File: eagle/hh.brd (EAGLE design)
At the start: 169.7 x 51.9 mm, 7 parts

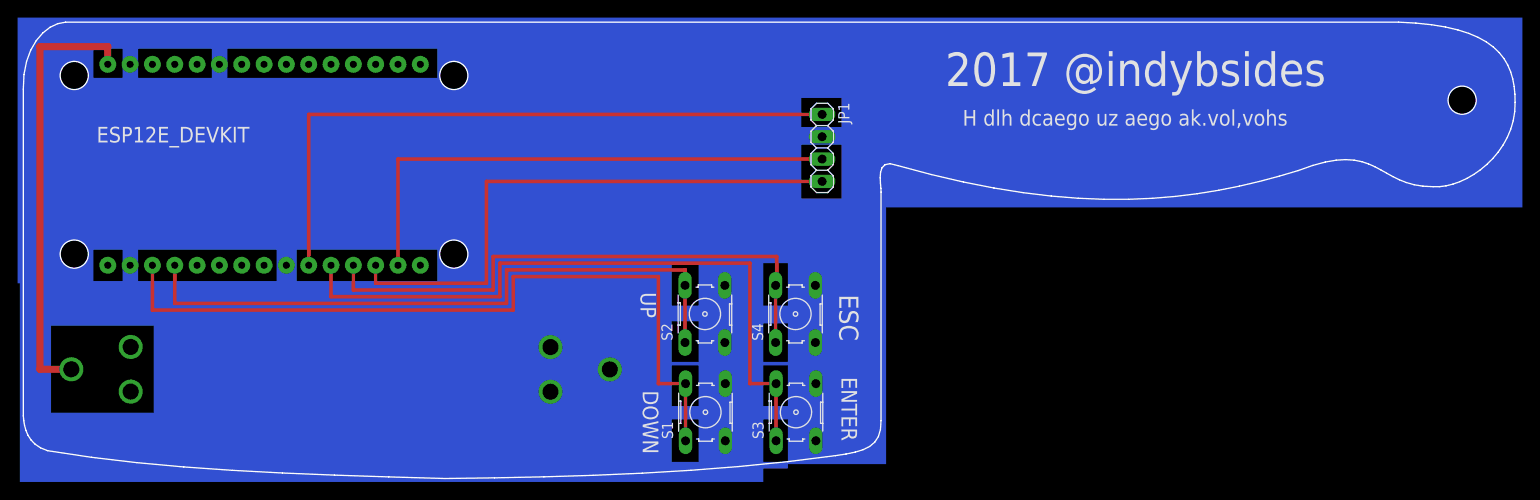
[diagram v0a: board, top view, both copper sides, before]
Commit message: Major changes to placement of components
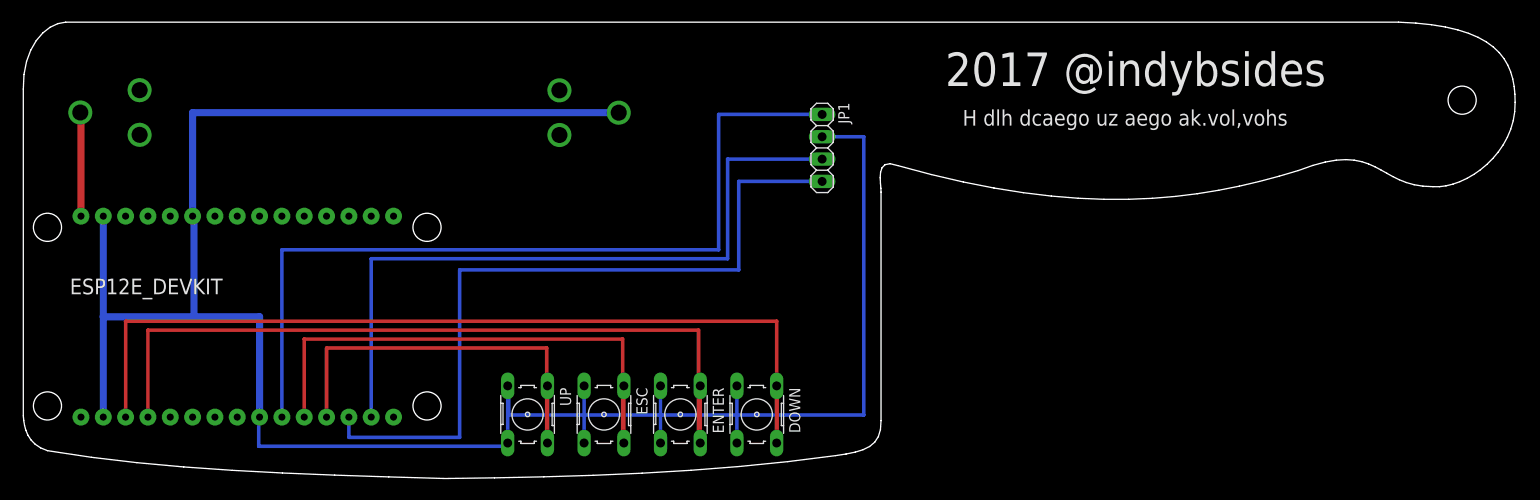
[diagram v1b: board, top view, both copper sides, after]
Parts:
- removed S1, S2, S3, S4: (no value), switch-omron:B3F-10XX
- added DOWN, ENTER, ESC, UP: (no value), switch-omron:B3F-10XX
- moved BAT1 29.2 mm to (37.3, 41.8)
- moved ESP12E_DEVKIT 17.5 mm to (24.5, 18.6)
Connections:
- net N$1: now also DOWN.3, DOWN.4, ENTER.3, ENTER.4, ESC.3, ESC.4, UP.3, UP.4; no longer S1.3, S1.4, S2.3, S2.4, S3.3, S3.4, S4.3, S4.4
- net N$2: now also UP.1, UP.2; no longer S4.1, S4.2
- net N$7: now also ESC.1, ESC.2; no longer S3.1, S3.2
- net N$8: now also ENTER.1, ENTER.2; no longer S2.1, S2.2
- net N$9: now also DOWN.1, DOWN.2; no longer S1.1, S1.2
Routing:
- net N$4: track 50.0 -> 11.9 mm
- net N$6: track 64.4 -> 85.3 mm
- net N$5: track 60.3 -> 80.6 mm
- net N$3: track 75.6 -> 95.9 mm
- net N$8: track 74.5 -> 92.1 mm
- net N$9: track 88.2 -> 105.3 mm
- net N$7: track 78.2 -> 63.6 mm
- net N$2: track 64.7 -> 50.3 mm
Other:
- board text removed: "DOWN"
- board text removed: "ENTER"
- board text removed: "ESC"
- board text removed: "UP"

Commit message: Trace Revisions
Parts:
- removed BAT1: (no value), SparkFun-Electromechanical:BATTERY_18650-HOLDER
- added BT1: (no value), SF_Batteries:BATTERY_18650-HOLDER
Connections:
- net N$1: now also BT1.GND@1; no longer BAT1.GND@1
- net N$4: now also BT1.PWR@1; no longer BAT1.PWR@1
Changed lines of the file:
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@@
 <layer number="113" name="IDFDebug" color="4" fill="1" visible="yes" active="yes"/>
 <layer number="116" name="Patch_BOT" color="9" fill="4" visible="yes" active="yes"/>
+<layer number="118" name="Rect_Pads" color="7" fill="1" visible="yes" active="yes"/>
 <layer number="121" name="_tsilk" color="7" fill="1" visible="yes" active="yes"/>
 <layer number="122" name="_bsilk" color="7" fill="1" visible="yes" active="yes"/>
@@
 <element name="ESP12E_DEVKIT" library="ESP12E_DEVKIT" package="ESP12E_DEVKIT" value="ESP12E_DEVKIT" x="24.482" y="18.558" rot="R270"/>
 <element name="JP1" library="pinhead" package="1X04" value="OLED" x="91.02" y="37.75" rot="R270"/>
-<element name="BAT1" library="SparkFun-Electromechanical" package="BATTERY_18650-HOLDER" value="" x="37.254" y="41.77" rot="SMR180"/>
+<element name="BT1" library="SF_Batteries" package="BATTERY_18650-HOLDER" value="" x="37.338" y="42.164" rot="SMR180">
+<attribute name="PROD_ID" value="BATT-12327" x="37.338" y="42.164" size="1.778" layer="28" rot="SMR180" display="off"/>
+<attribute name="SF_SKU" value="PRT-13113" x="37.338" y="42.164" size="1.778" layer="28" rot="SMR180" display="off"/>
+</element>
 </elements>
 <signals>
@@
 <contactref element="ESC" pad="4"/>
 <contactref element="UP" pad="4"/>
-<contactref element="BAT1" pad="GND@1"/>
 <wire x1="63.9414" y1="10.6812" x2="63.9414" y2="4.1788" width="0.4064" layer="16"/>
 <wire x1="81.3254" y1="7.366" x2="81.3254" y2="10.6812" width="0.4064" layer="16"/>
@@
 <wire x1="55.2494" y1="4.1788" x2="55.2494" y2="10.6812" width="0.4064" layer="16"/>
 <wire x1="9.242" y1="7.128" x2="9.242" y2="18.542" width="0.8128" layer="16"/>
-<wire x1="19.402" y1="29.988" x2="19.558" y2="29.988" width="0.4064" layer="16"/>
-<wire x1="19.558" y1="29.988" x2="19.558" y2="18.542" width="0.8128" layer="16"/>
-<wire x1="19.558" y1="18.542" x2="9.242" y2="18.542" width="0.8128" layer="16"/>
+<wire x1="19.402" y1="29.988" x2="19.304" y2="29.988" width="0.4064" layer="16"/>
+<wire x1="19.304" y1="29.988" x2="19.304" y2="18.542" width="0.8128" layer="16"/>
+<wire x1="19.304" y1="18.542" x2="9.242" y2="18.542" width="0.8128" layer="16"/>
 <wire x1="9.242" y1="18.542" x2="9.242" y2="29.988" width="0.8128" layer="16"/>
-<wire x1="19.558" y1="18.542" x2="27.022" y2="18.542" width="0.8128" layer="16"/>
+<wire x1="19.304" y1="18.542" x2="27.022" y2="18.542" width="0.8128" layer="16"/>
 <wire x1="27.022" y1="18.542" x2="27.022" y2="7.128" width="0.8128" layer="16"/>
 <wire x1="55.2494" y1="10.6812" x2="55.372" y2="10.6812" width="0.4064" layer="16"/>
@@
 <wire x1="95.758" y1="39.02" x2="95.758" y2="7.366" width="0.4064" layer="16"/>
 <wire x1="95.758" y1="7.366" x2="81.3254" y2="7.366" width="0.4064" layer="16"/>
-<wire x1="67.882" y1="41.76" x2="19.402" y2="41.76" width="0.8128" layer="16"/>
-<wire x1="19.402" y1="41.76" x2="19.402" y2="29.988" width="0.8128" layer="16"/>
+<contactref element="BT1" pad="GND@1"/>
+<wire x1="67.966" y1="42.154" x2="67.818" y2="42.154" width="0.4064" layer="1"/>
+<wire x1="67.818" y1="42.154" x2="67.818" y2="33.782" width="0.8128" layer="1"/>
+<wire x1="67.818" y1="33.782" x2="19.402" y2="33.782" width="0.8128" layer="1"/>
+<wire x1="19.402" y1="33.782" x2="19.402" y2="29.988" width="0.8128" layer="1"/>
 <wire x1="63.9414" y1="10.6812" x2="72.6334" y2="10.6812" width="0" layer="19" extent="1-1"/>
 <wire x1="55.372" y1="10.6812" x2="63.9414" y2="10.6812" width="0" layer="19" extent="16-16"/>
 </signal>
 <signal name="N$4">
-<contactref element="BAT1" pad="PWR@1"/>
+<contactref element="BT1" pad="PWR@1"/>
 <contactref element="ESP12E_DEVKIT" pad="VIN"/>
-<wire x1="6.626" y1="41.78" x2="6.702" y2="41.78" width="0.8128" layer="1"/>
-<wire x1="6.702" y1="41.78" x2="6.702" y2="29.988" width="0.8128" layer="1"/>
+<wire x1="6.71" y1="42.174" x2="6.702" y2="42.174" width="0.4064" layer="1"/>
+<wire x1="6.702" y1="42.174" x2="6.702" y2="29.988" width="0.8128" layer="1"/>
 </signal>
 </signals>

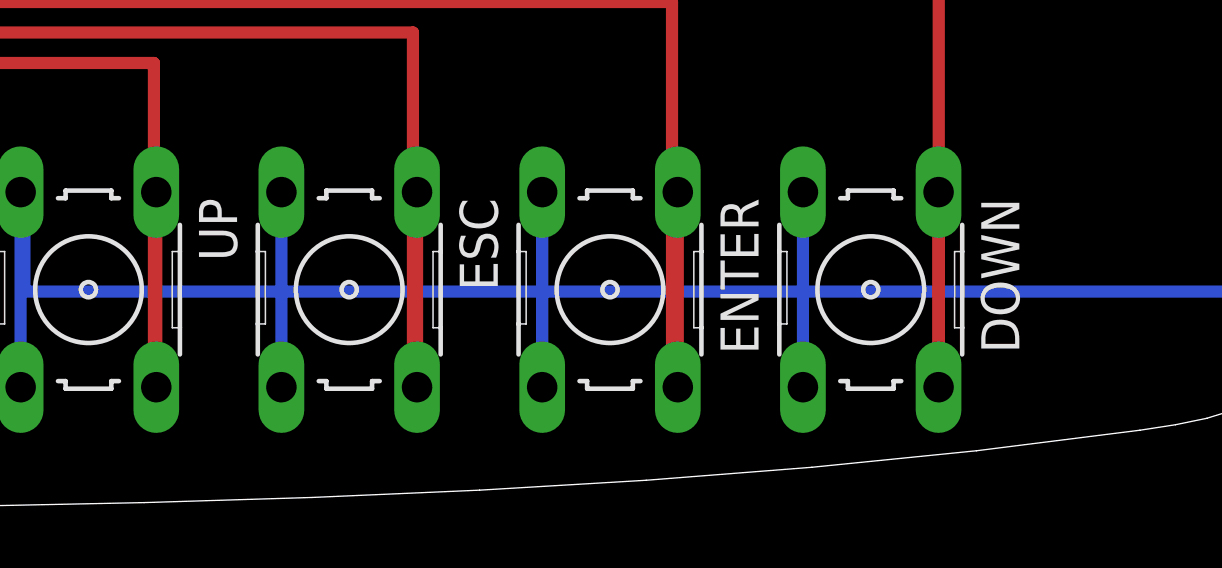
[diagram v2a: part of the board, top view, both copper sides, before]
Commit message: silkscreen edits
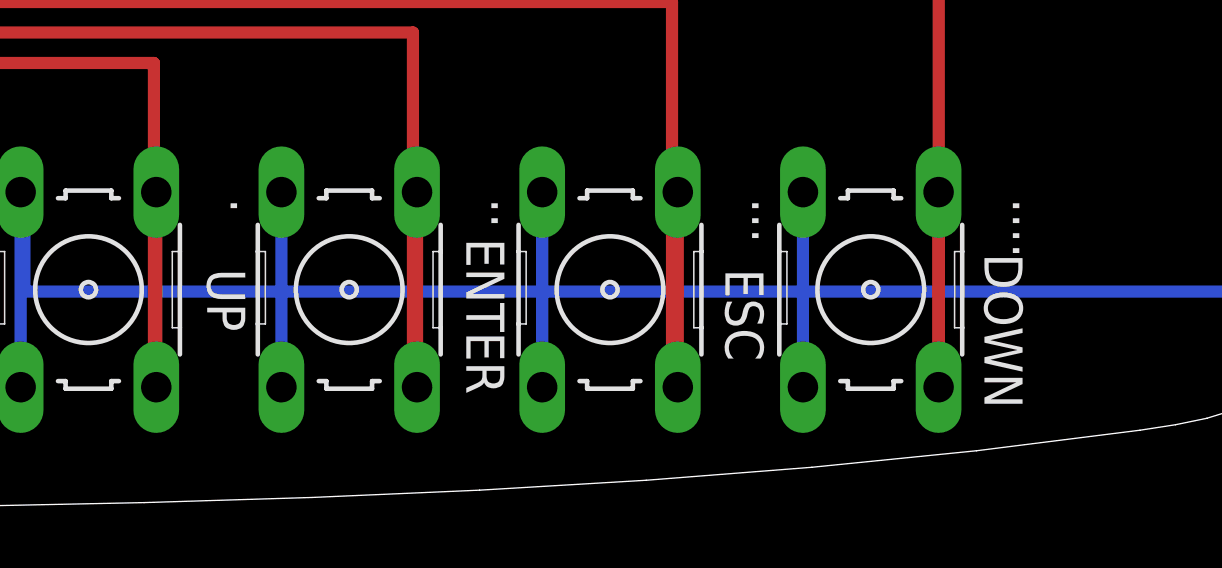
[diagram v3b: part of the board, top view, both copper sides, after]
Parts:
- renumbered DOWN to ...., ENTER to ..., ESC to .., UP to .
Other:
- board text added: "DOWN"
- board text added: "ENTER"
- board text added: "ESC"
- board text added: "UP"
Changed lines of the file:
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@@
 <text x="161.292" y="45.222" size="3.81" layer="22" font="vector" rot="MR0">@p0lr_ @theDevilsVoice</text>
 <text x="107" y="40.286" size="1.778" layer="21" font="vector">H dlh dcaego uz aego ak.vol,vohs</text>
+<text x="61.468" y="8.128" size="1.27" layer="21" rot="SR270">UP</text>
+<text x="87.376" y="8.636" size="1.27" layer="21" rot="SR270">DOWN</text>
+<text x="70.104" y="9.144" size="1.27" layer="21" rot="SR270">ENTER</text>
+<text x="78.74" y="8.128" size="1.27" layer="21" rot="SR270">ESC</text>
 </plain>
 <attributes>
@@
 </autorouter>
 <elements>
-<element name="DOWN" library="switch-omron" package="B3F-10XX" value="" x="83.586" y="7.43" rot="R270">
+<element name="...." library="switch-omron" package="B3F-10XX" value="" x="83.586" y="7.43" rot="R270">
 <attribute name="OC_NEWARK" value="36M3542" x="83.586" y="7.43" size="1.778" layer="27" rot="R270" display="off"/>
 <attribute name="MPN" value="B3F-1000" x="83.586" y="7.43" size="1.778" layer="27" rot="R270" display="off"/>
@@
 <attribute name="OC_FARNELL" value="176432" x="83.586" y="7.43" size="1.778" layer="27" rot="R270" display="off"/>
 </element>
-<element name="ENTER" library="switch-omron" package="B3F-10XX" value="" x="74.894" y="7.43" rot="R270">
+<element name="..." library="switch-omron" package="B3F-10XX" value="" x="74.894" y="7.43" rot="R270">
 <attribute name="OC_NEWARK" value="36M3542" x="74.894" y="7.43" size="1.778" layer="27" rot="R270" display="off"/>
 <attribute name="MPN" value="B3F-1000" x="74.894" y="7.43" size="1.778" layer="27" rot="R270" display="off"/>
@@
 <attribute name="OC_FARNELL" value="176432" x="74.894" y="7.43" size="1.778" layer="27" rot="R270" display="off"/>
 </element>
-<element name="ESC" library="switch-omron" package="B3F-10XX" value="" x="66.202" y="7.43" rot="R270">
+<element name=".." library="switch-omron" package="B3F-10XX" value="" x="66.202" y="7.43" rot="R270">
 <attribute name="OC_NEWARK" value="36M3542" x="66.202" y="7.43" size="1.778" layer="27" rot="R270" display="off"/>
 <attribute name="MPN" value="B3F-1000" x="66.202" y="7.43" size="1.778" layer="27" rot="R270" display="off"/>
@@
 <attribute name="OC_FARNELL" value="176432" x="66.202" y="7.43" size="1.778" layer="27" rot="R270" display="off"/>
 </element>
-<element name="UP" library="switch-omron" package="B3F-10XX" value="" x="57.51" y="7.43" rot="R270">
+<element name="." library="switch-omron" package="B3F-10XX" value="" x="57.51" y="7.43" rot="R270">
 <attribute name="OC_NEWARK" value="36M3542" x="57.51" y="7.43" size="1.778" layer="27" rot="R270" display="off"/>
 <attribute name="MPN" value="B3F-1000" x="57.51" y="7.43" size="1.778" layer="27" rot="R270" display="off"/>
@@
 <signal name="N$2">
 <contactref element="ESP12E_DEVKIT" pad="D3"/>
-<contactref element="UP" pad="2"/>
-<contactref element="UP" pad="1"/>
+<contactref element="." pad="2"/>
+<contactref element="." pad="1"/>
 <wire x1="59.7706" y1="10.6812" x2="59.7706" y2="4.1788" width="0.4064" layer="1"/>
 <wire x1="59.7706" y1="4.1788" x2="59.69" y2="4.1788" width="0.4064" layer="1"/>
@@
 <signal name="N$7">
 <contactref element="ESP12E_DEVKIT" pad="D4"/>
-<contactref element="ESC" pad="2"/>
-<contactref element="ESC" pad="1"/>
+<contactref element=".." pad="2"/>
+<contactref element=".." pad="1"/>
 <wire x1="68.4626" y1="10.6812" x2="68.4626" y2="4.1788" width="0.4064" layer="1"/>
 <wire x1="68.4626" y1="4.1788" x2="68.326" y2="4.1788" width="0.4064" layer="1"/>
@@
 </signal>
 <signal name="N$8">
-<contactref element="ENTER" pad="2"/>
-<contactref element="ENTER" pad="1"/>
+<contactref element="..." pad="2"/>
+<contactref element="..." pad="1"/>
 <contactref element="ESP12E_DEVKIT" pad="RX"/>
 <wire x1="77.1546" y1="10.6812" x2="77.1546" y2="4.1788" width="0.4064" layer="1"/>
@@
 </signal>
 <signal name="N$9">
-<contactref element="DOWN" pad="2"/>
-<contactref element="DOWN" pad="1"/>
+<contactref element="...." pad="2"/>
+<contactref element="...." pad="1"/>
 <contactref element="ESP12E_DEVKIT" pad="TX"/>
 <wire x1="85.8466" y1="10.6812" x2="85.8466" y2="4.1788" width="0.4064" layer="1"/>
@@
 <contactref element="JP1" pad="2"/>
 <contactref element="ESP12E_DEVKIT" pad="GND@2"/>
-<contactref element="UP" pad="3"/>
-<contactref element="ESC" pad="3"/>
-<contactref element="ENTER" pad="3"/>
-<contactref element="DOWN" pad="3"/>
-<contactref element="DOWN" pad="4"/>
-<contactref element="ENTER" pad="4"/>
-<contactref element="ESC" pad="4"/>
-<contactref element="UP" pad="4"/>
+<contactref element="." pad="3"/>
+<contactref element=".." pad="3"/>
+<contactref element="..." pad="3"/>
+<contactref element="...." pad="3"/>
+<contactref element="...." pad="4"/>
+<contactref element="..." pad="4"/>
+<contactref element=".." pad="4"/>
+<contactref element="." pad="4"/>
 <wire x1="63.9414" y1="10.6812" x2="63.9414" y2="4.1788" width="0.4064" layer="16"/>
 <wire x1="81.3254" y1="7.366" x2="81.3254" y2="10.6812" width="0.4064" layer="16"/>
